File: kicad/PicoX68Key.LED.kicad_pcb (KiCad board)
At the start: 2 copper layers, 33.9 x 42.2 mm, 23 parts, among them J1 LED_BOARD, U1 74HCT595, U2 74HCT595

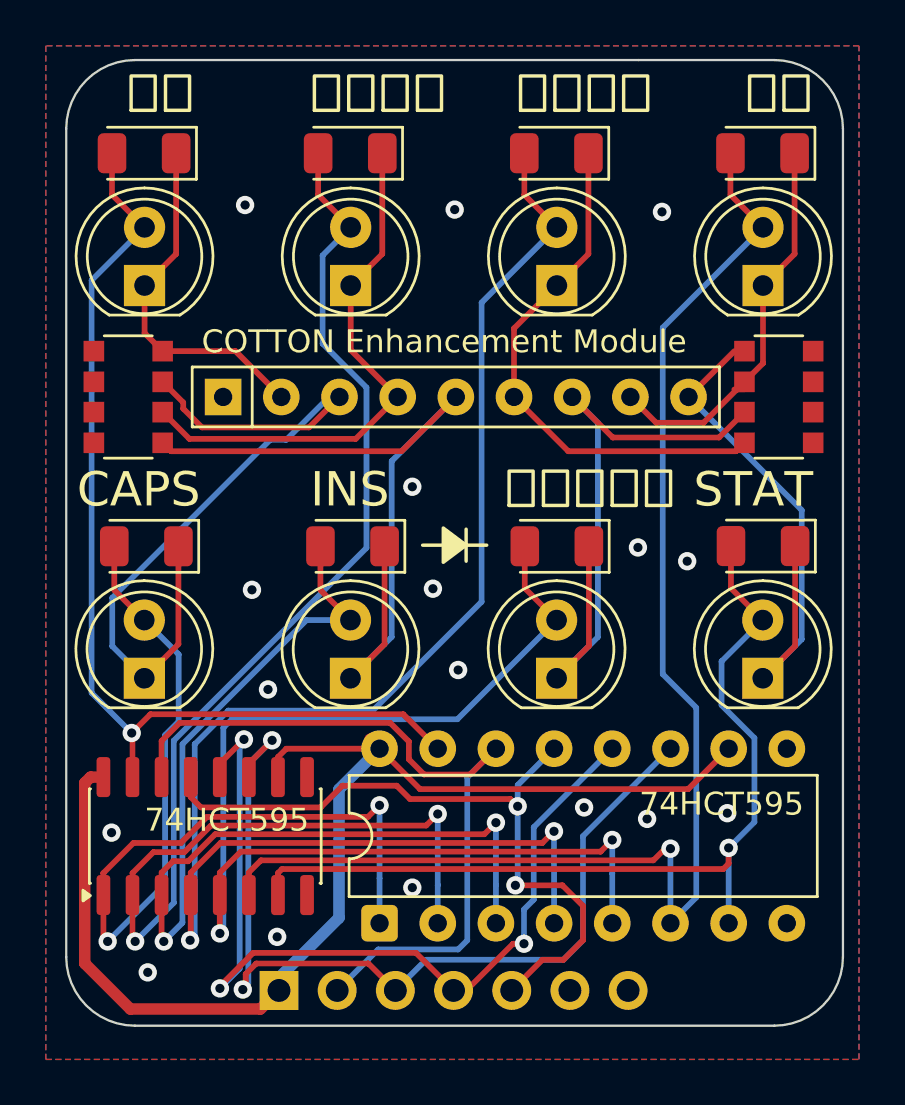
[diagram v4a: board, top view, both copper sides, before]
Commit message: Changes to enable brightness control. Final PCB polish.
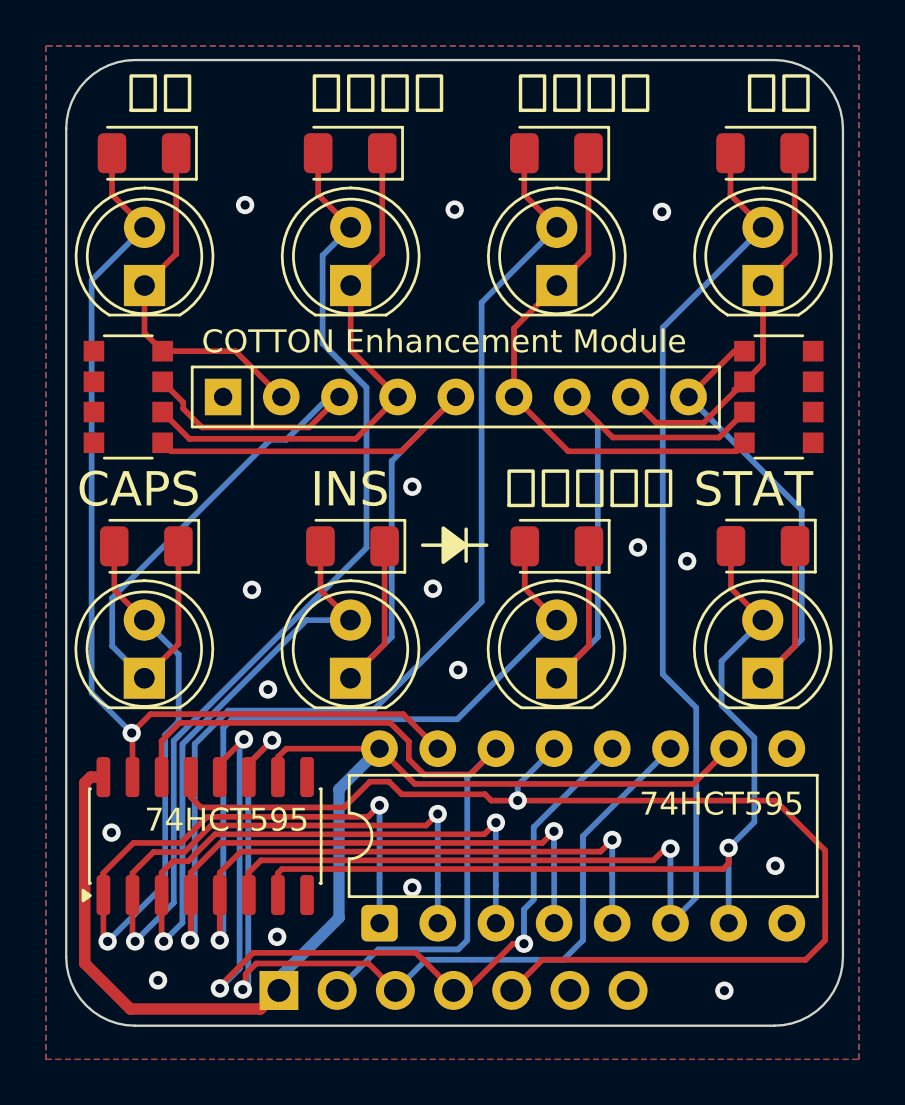
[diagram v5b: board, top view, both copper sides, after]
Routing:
- net /OE: track 31.6 -> 51.9 mm, vias 2 -> 1
- net GND: vias 17 -> 16
